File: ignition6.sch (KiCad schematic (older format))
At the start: 9 parts, among them P6 CONN_1, P7 CONN_1, Q1 MOSFET_N, SW1 SWITCH_INV

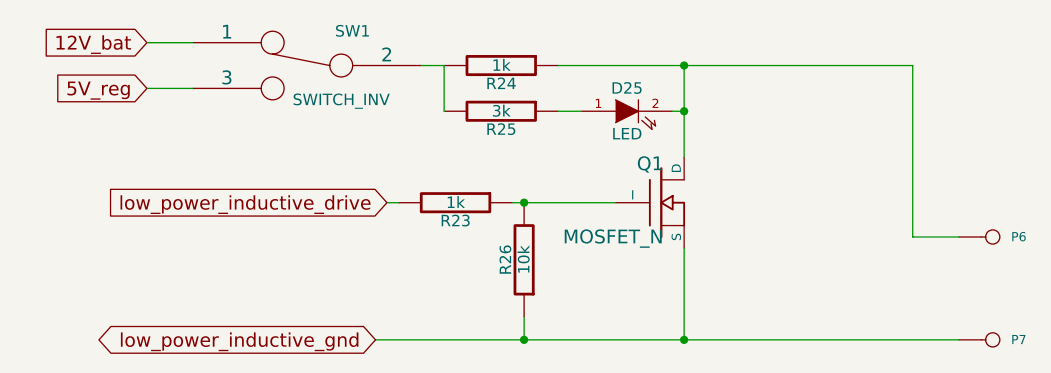
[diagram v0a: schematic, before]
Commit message: Removed LM1815 options. Now adaptive mode and square waves are the default,
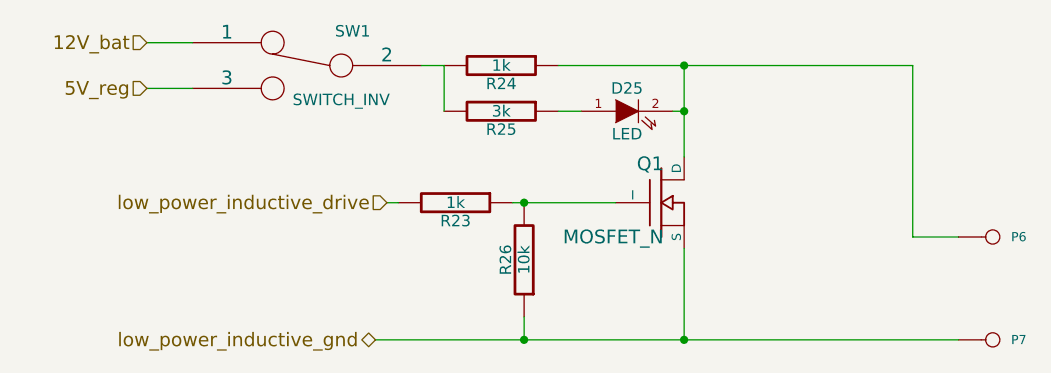
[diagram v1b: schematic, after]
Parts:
- D25: Field1 (none) -> newark,58k2469; Field2 (none) -> vendor1, smd w hem; Field3 (none) -> vendor2, thru w hem; Field4 (none) -> vendor2, smd w hem; Field5 (none) -> x,x; Field6 (none) -> x,x; Field7 (none) -> green; Field8 (none) -> other,more,stuff
- Q1: Field1 (none) -> digi,PIP3104-ND; Field2 (none) -> vendor1, smd w hem; Field3 (none) -> vendor2, thru w hem; Field4 (none) -> vendor2, smd w hem; Field5 (none) -> 8,A; Field6 (none) -> x,x; Field7 (none) -> TOPFET; Field8 (none) -> other,more,stuff
- R23, R24: Field1 (none) -> newark,38k0327; Field2 (none) -> vendor1, smd w hem; Field3 (none) -> vendor2, thru w hem; Field4 (none) -> vendor2, smd w hem; Field5 (none) -> 250,mW; Field6 (none) -> 5,%; Field7 (none) -> carbon film; Field8 (none) -> other,more,stuff
- R25: Field1 (none) -> newark,38k0340; Field2 (none) -> vendor1, smd w hem; Field3 (none) -> vendor2, thru w hem; Field4 (none) -> vendor2, smd w hem; Field5 (none) -> 1/4,W; Field6 (none) -> 5,%; Field7 (none) -> carbon film; Field8 (none) -> other,more,stuff
- R26: Field1 (none) -> newark,38k0328; Field2 (none) -> vendor1, smd w hem; Field3 (none) -> vendor2, thru w hem; Field4 (none) -> vendor2, smd w hem; Field5 (none) -> 250,mW; Field6 (none) -> 5,%; Field7 (none) -> carbon film; Field8 (none) -> other,more,stuff
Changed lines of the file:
@@
-EESchema Schematic File Version 1
-LIBS:power,./freeEMS_lib,device,conn,linear,regul,74xx,cmos4000,adc-dac,memory,xilinx,special,microcontrollers,dsp,microchip,analog_switches,motorola,texas,intel,audio,interface,digital-audio,philips,display,cypress,siliconi,contrib,valves,./freeEMS_1.cache
+EESchema Schematic File Version 2  date Fri 02 Jul 2010 02:24:35 PM ART
+LIBS:power
+LIBS:freeEMS_lib
+LIBS:device
+LIBS:conn
+LIBS:linear
+LIBS:regul
+LIBS:74xx
+LIBS:cmos4000
+LIBS:adc-dac
+LIBS:memory
+LIBS:xilinx
+LIBS:special
+LIBS:microcontrollers
+LIBS:dsp
+LIBS:microchip
+LIBS:analog_switches
+LIBS:motorola
+LIBS:texas
+LIBS:intel
+LIBS:audio
+LIBS:interface
+LIBS:digital-audio
+LIBS:philips
+LIBS:display
+LIBS:cypress
+LIBS:siliconi
+LIBS:contrib
+LIBS:valves
+LIBS:freeEMS_1-cache
 EELAYER 23  0
 EELAYER END
@@
 Sheet 10 41
 Title "freeEMS 1.0"
-Date "15 nov 2008"
+Date "2 jul 2010"
 Rev "A.20"
 Comp "diyefi.org"
@@
 U 1 1 48B16ED5
 P 4000 2050
-F 0 "Q1" H 4010 2220 60  0000 R C
-F 1 "MOSFET_N" H 4010 1900 60  0000 R C
-F 2 "TO220_sm" V 3930 2800 60  0001 C C
-F 4 "digi,PIP3104-ND" V 2130 3800 60  0001 C C
-F 5 "vendor1, smd w hem" V 2130 3800 60  0001 C C
-F 6 "vendor2, thru w hem" V 2130 3800 60  0001 C C
-F 7 "vendor2, smd w hem" V 2130 3800 60  0001 C C
-F 8 "8,A" V 2130 3800 60  0001 C C
-F 9 "x,x" V 2130 3800 60  0001 C C
-F 10 "TOPFET" V 2130 3800 60  0001 C C
-F 11 "other,more,stuff" V 2130 3800 60  0001 C C
+F 0 "Q1" H 4010 2220 60  0000 R CNN
+F 1 "MOSFET_N" H 4010 1900 60  0000 R CNN
+F 2 "TO220_sm" V 3930 2800 60  0001 C CNN
+F 4 "digi,PIP3104-ND" V 2130 3800 60  0001 C CNN "Field1"
+F 5 "vendor1, smd w hem" V 2130 3800 60  0001 C CNN "Field2"
+F 6 "vendor2, thru w hem" V 2130 3800 60  0001 C CNN "Field3"
+F 7 "vendor2, smd w hem" V 2130 3800 60  0001 C CNN "Field4"
+F 8 "8,A" V 2130 3800 60  0001 C CNN "Field5"
+F 9 "x,x" V 2130 3800 60  0001 C CNN "Field6"
+F 10 "TOPFET" V 2130 3800 60  0001 C CNN "Field7"
+F 11 "other,more,stuff" V 2130 3800 60  0001 C CNN "Field8"
 	1    4000 2050
 	1    0    0    -1
@@
 U 1 1 48AE08BB
 P 3400 2300
-F 0 "R26" V 3480 2300 50  0000 C C
-F 1 "10k" V 3400 2300 50  0000 C C
-F 2 "R4-SM0805" V 3580 2400 60  0001 C C
-F 4 "newark,38k0328" V 1230 2850 60  0001 C C
-F 5 "vendor1, smd w hem" V 1230 2850 60  0001 C C
-F 6 "vendor2, thru w hem" V 1230 2850 60  0001 C C
-F 7 "vendor2, smd w hem" V 1230 2850 60  0001 C C
-F 8 "250,mW" V 1230 2850 60  0001 C C
-F 9 "5,%" V 1230 2850 60  0001 C C
-F 10 "carbon film" V 1230 2850 60  0001 C C
-F 11 "other,more,stuff" V 1230 2850 60  0001 C C
+F 0 "R26" V 3480 2300 50  0000 C CNN
+F 1 "10k" V 3400 2300 50  0000 C CNN
+F 2 "R4-SM0805" V 3580 2400 60  0001 C CNN
+F 4 "newark,38k0328" V 1230 2850 60  0001 C CNN "Field1"
+F 5 "vendor1, smd w hem" V 1230 2850 60  0001 C CNN "Field2"
+F 6 "vendor2, thru w hem" V 1230 2850 60  0001 C CNN "Field3"
+F 7 "vendor2, smd w hem" V 1230 2850 60  0001 C CNN "Field4"
+F 8 "250,mW" V 1230 2850 60  0001 C CNN "Field5"
+F 9 "5,%" V 1230 2850 60  0001 C CNN "Field6"
+F 10 "carbon film" V 1230 2850 60  0001 C CNN "Field7"
+F 11 "other,more,stuff" V 1230 2850 60  0001 C CNN "Field8"
 	1    3400 2300
 	-1   0    0    1
@@
 U 1 1 48AE0832
 P 2450 1450
-F 0 "SW1" H 2250 1600 50  0000 C C
-F 1 "SWITCH_INV" H 2300 1300 50  0000 C C
-F 2 "SIL-3" H 2350 1700 60  0001 C C
+F 0 "SW1" H 2250 1600 50  0000 C CNN
+F 1 "SWITCH_INV" H 2300 1300 50  0000 C CNN
+F 2 "SIL-3" H 2350 1700 60  0001 C CNN
 	1    2450 1450
 	-1   0    0    -1
@@
 U 1 1 48AA2529
 P 3850 1650
-F 0 "D25" H 3850 1750 50  0000 C C
-F 1 "LED" H 3850 1550 50  0000 C C
-F 2 "LEDV" V 1680 5050 60  0001 C C
-F 4 "newark,58k2469" V 430 2100 60  0001 C C
-F 5 "vendor1, smd w hem" V 430 2100 60  0001 C C
-F 6 "vendor2, thru w hem" V 430 2100 60  0001 C C
-F 7 "vendor2, smd w hem" V 430 2100 60  0001 C C
-F 8 "x,x" V 430 2100 60  0001 C C
-F 9 "x,x" V 430 2100 60  0001 C C
-F 10 "green" V 430 2100 60  0001 C C
-F 11 "other,more,stuff" V 430 2100 60  0001 C C
+F 0 "D25" H 3850 1750 50  0000 C CNN
+F 1 "LED" H 3850 1550 50  0000 C CNN
+F 2 "LEDV" V 1680 5050 60  0001 C CNN
+F 4 "newark,58k2469" V 430 2100 60  0001 C CNN "Field1"
+F 5 "vendor1, smd w hem" V 430 2100 60  0001 C CNN "Field2"
+F 6 "vendor2, thru w hem" V 430 2100 60  0001 C CNN "Field3"
+F 7 "vendor2, smd w hem" V 430 2100 60  0001 C CNN "Field4"
+F 8 "x,x" V 430 2100 60  0001 C CNN "Field5"
+F 9 "x,x" V 430 2100 60  0001 C CNN "Field6"
+F 10 "green" V 430 2100 60  0001 C CNN "Field7"
+F 11 "other,more,stuff" V 430 2100 60  0001 C CNN "Field8"
 	1    3850 1650
 	1    0    0    -1
@@
 U 1 1 48AA2523
 P 3300 1650
-F 0 "R25" V 3380 1650 50  0000 C C
-F 1 "3k" V 3300 1650 50  0000 C C
-F 2 "R4-SM0805" V 1980 1650 60  0001 C C
-F 4 "newark,38k0340" V -120 2400 60  0001 C C
-F 5 "vendor1, smd w hem" V -120 2400 60  0001 C C
-F 6 "vendor2, thru w hem" V -120 2400 60  0001 C C
-F 7 "vendor2, smd w hem" V -120 2400 60  0001 C C
-F 8 "1/4,W" V -120 2400 60  0001 C C
-F 9 "5,%" V -120 2400 60  0001 C C
-F 10 "carbon film" V -120 2400 60  0001 C C
-F 11 "other,more,stuff" V -120 2400 60  0001 C C
+F 0 "R25" V 3380 1650 50  0000 C CNN
+F 1 "3k" V 3300 1650 50  0000 C CNN
+F 2 "R4-SM0805" V 1980 1650 60  0001 C CNN
+F 4 "newark,38k0340" V -120 2400 60  0001 C CNN "Field1"
+F 5 "vendor1, smd w hem" V -120 2400 60  0001 C CNN "Field2"
+F 6 "vendor2, thru w hem" V -120 2400 60  0001 C CNN "Field3"
+F 7 "vendor2, smd w hem" V -120 2400 60  0001 C CNN "Field4"
+F 8 "1/4,W" V -120 2400 60  0001 C CNN "Field5"
+F 9 "5,%" V -120 2400 60  0001 C CNN "Field6"
+F 10 "carbon film" V -120 2400 60  0001 C CNN "Field7"
+F 11 "other,more,stuff" V -120 2400 60  0001 C CNN "Field8"
 	1    3300 1650
 	0    1    1    0
@@
 U 1 1 48AA1A4E
 P 5450 2650
-F 0 "P7" H 5530 2650 40  0000 L C
-F 1 "CONN_1" H 5450 2705 30  0001 C C
-F 2 "1PIN" V 1880 2850 60  0001 C C
+F 0 "P7" H 5530 2650 40  0000 L CNN
+F 1 "CONN_1" H 5450 2705 30  0001 C CNN
+F 2 "1PIN" V 1880 2850 60  0001 C CNN
 	1    5450 2650
 	1    0    0    -1
@@
 U 1 1 48AA1A4A
 P 5450 2200
-F 0 "P6" H 5530 2200 40  0000 L C
-F 1 "CONN_1" H 5450 2255 30  0001 C C
-F 2 "1PIN" V 1880 2600 60  0001 C C
+F 0 "P6" H 5530 2200 40  0000 L CNN
+F 1 "CONN_1" H 5450 2255 30  0001 C CNN
+F 2 "1PIN" V 1880 2600 60  0001 C CNN
 	1    5450 2200
 	1    0    0    -1
 $EndComp
-Text GLabel 1750 1550 0    60   Input
+Text HLabel 1750 1550 0    60   Input ~ 0
 5V_reg
 $Comp
@@
 U 1 1 489395E6
 P 3100 2050
-F 0 "R23" V 3180 2050 50  0000 C C
-F 1 "1k" V 3100 2050 50  0000 C C
-F 2 "R4-SM0805" V 3280 2150 60  0001 C C
-F 4 "newark,38k0327" V 930 2600 60  0001 C C
-F 5 "vendor1, smd w hem" V 930 2600 60  0001 C C
-F 6 "vendor2, thru w hem" V 930 2600 60  0001 C C
-F 7 "vendor2, smd w hem" V 930 2600 60  0001 C C
-F 8 "250,mW" V 930 2600 60  0001 C C
-F 9 "5,%" V 930 2600 60  0001 C C
-F 10 "carbon film" V 930 2600 60  0001 C C
-F 11 "other,more,stuff" V 930 2600 60  0001 C C
+F 0 "R23" V 3180 2050 50  0000 C CNN
+F 1 "1k" V 3100 2050 50  0000 C CNN
+F 2 "R4-SM0805" V 3280 2150 60  0001 C CNN
+F 4 "newark,38k0327" V 930 2600 60  0001 C CNN "Field1"
+F 5 "vendor1, smd w hem" V 930 2600 60  0001 C CNN "Field2"
+F 6 "vendor2, thru w hem" V 930 2600 60  0001 C CNN "Field3"
+F 7 "vendor2, smd w hem" V 930 2600 60  0001 C CNN "Field4"
+F 8 "250,mW" V 930 2600 60  0001 C CNN "Field5"
+F 9 "5,%" V 930 2600 60  0001 C CNN "Field6"
+F 10 "carbon film" V 930 2600 60  0001 C CNN "Field7"
+F 11 "other,more,stuff" V 930 2600 60  0001 C CNN "Field8"
 	1    3100 2050
 	0    1    1    0
@@
 U 1 1 489395D4
 P 3300 1450
-F 0 "R24" V 3380 1450 50  0000 C C
-F 1 "1k" V 3300 1450 50  0000 C C
-F 2 "R4-SM0805" V 3480 1550 60  0001 C C
-F 4 "newark,38k0327" V 1130 2350 60  0001 C C
-F 5 "vendor1, smd w hem" V 1130 2350 60  0001 C C
-F 6 "vendor2, thru w hem" V 1130 2350 60  0001 C C
-F 7 "vendor2, smd w hem" V 1130 2350 60  0001 C C
-F 8 "250,mW" V 1130 2350 60  0001 C C
-F 9 "5,%" V 1130 2350 60  0001 C C
-F 10 "carbon film" V 1130 2350 60  0001 C C
-F 11 "other,more,stuff" V 1130 2350 60  0001 C C
+F 0 "R24" V 3380 1450 50  0000 C CNN
+F 1 "1k" V 3300 1450 50  0000 C CNN
+F 2 "R4-SM0805" V 3480 1550 60  0001 C CNN
+F 4 "newark,38k0327" V 1130 2350 60  0001 C CNN "Field1"
+F 5 "vendor1, smd w hem" V 1130 2350 60  0001 C CNN "Field2"
+F 6 "vendor2, thru w hem" V 1130 2350 60  0001 C CNN "Field3"
+F 7 "vendor2, smd w hem" V 1130 2350 60  0001 C CNN "Field4"
+F 8 "250,mW" V 1130 2350 60  0001 C CNN "Field5"
+F 9 "5,%" V 1130 2350 60  0001 C CNN "Field6"
+F 10 "carbon film" V 1130 2350 60  0001 C CNN "Field7"
+F 11 "other,more,stuff" V 1130 2350 60  0001 C CNN "Field8"
 	1    3300 1450
 	0    1    1    0
 $EndComp
-Text GLabel 1750 1350 0    60   Input
+Text HLabel 1750 1350 0    60   Input ~ 0
 12V_bat
-Text GLabel 2750 2650 0    60   BiDi
+Text HLabel 2750 2650 0    60   BiDi ~ 0
 low_power_inductive_gnd
-Text GLabel 2800 2050 0    60   Input
+Text HLabel 2800 2050 0    60   Input ~ 0
 low_power_inductive_drive
 $EndSCHEMATC

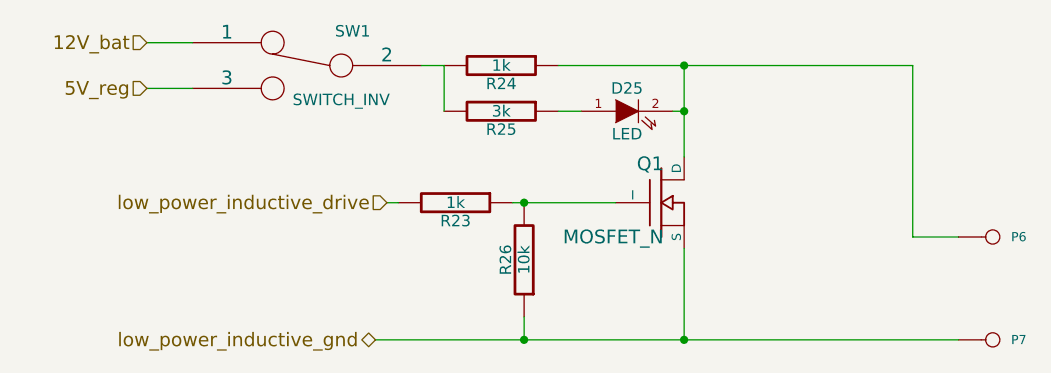
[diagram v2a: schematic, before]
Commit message: Implemented P&H, removed current sense circuitry, removed all unnecessary files from the repo
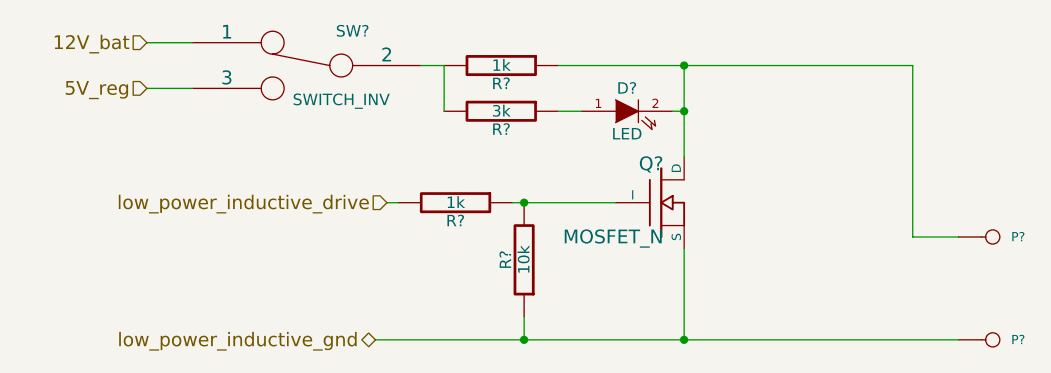
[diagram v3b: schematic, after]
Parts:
- R?: renamed from R26; Field1 newark,38k0328 -> newark,38K0328
- renumbered D25 to D?, P6 to P?, P7 to P?, Q1 to Q?, R24 to R?, R23 to R?, R25 to R?, SW1 to SW?
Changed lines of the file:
@@
-EESchema Schematic File Version 2  date Fri 02 Jul 2010 05:44:26 PM ART
+EESchema Schematic File Version 2  date Sat 03 Jul 2010 10:49:02 AM ART
 LIBS:power
 LIBS:freeEMS_lib
@@
 EELAYER END
 $Descr A4 11700 8267
-Sheet 10 41
+Sheet 1 41
 Title "freeEMS 1.0"
-Date "2 jul 2010"
-Rev "A.20"
+Date "3 jul 2010"
+Rev "A.07"
 Comp "diyefi.org"
 Comment1 "ignition.sch"
@@
 Connection ~ 3400 2050
 $Comp
-L PIP-3104 Q1
+L PIP-3104 Q?
 U 1 1 48B16ED5
 P 4000 2050
-F 0 "Q1" H 4010 2220 60  0000 R CNN
+F 0 "Q?" H 4010 2220 60  0000 R CNN
 F 1 "MOSFET_N" H 4010 1900 60  0000 R CNN
 F 2 "TO220_sm" V 3930 2800 60  0001 C CNN
@@
 $EndComp
 $Comp
-L R R26
+L R R?
 U 1 1 48AE08BB
 P 3400 2300
-F 0 "R26" V 3480 2300 50  0000 C CNN
+F 0 "R?" V 3480 2300 50  0000 C CNN
 F 1 "10k" V 3400 2300 50  0000 C CNN
 F 2 "R4-SM0805" V 3580 2400 60  0001 C CNN
-F 4 "newark,38k0328" V 1230 2850 60  0001 C CNN "Field1"
+F 4 "newark,38K0328" V 1230 2850 60  0001 C CNN "Field1"
 F 5 "vendor1, smd w hem" V 1230 2850 60  0001 C CNN "Field2"
 F 6 "vendor2, thru w hem" V 1230 2850 60  0001 C CNN "Field3"
@@
 $EndComp
 $Comp
-L SWITCH_INV SW1
+L SWITCH_INV SW?
 U 1 1 48AE0832
 P 2450 1450
-F 0 "SW1" H 2250 1600 50  0000 C CNN
+F 0 "SW?" H 2250 1600 50  0000 C CNN
 F 1 "SWITCH_INV" H 2300 1300 50  0000 C CNN
 F 2 "SIL-3" H 2350 1700 60  0001 C CNN
@@
 $EndComp
 $Comp
-L LED D25
+L LED D?
 U 1 1 48AA2529
 P 3850 1650
-F 0 "D25" H 3850 1750 50  0000 C CNN
+F 0 "D?" H 3850 1750 50  0000 C CNN
 F 1 "LED" H 3850 1550 50  0000 C CNN
 F 2 "LEDV" V 1680 5050 60  0001 C CNN
@@
 $EndComp
 $Comp
-L R R25
+L R R?
 U 1 1 48AA2523
 P 3300 1650
-F 0 "R25" V 3380 1650 50  0000 C CNN
+F 0 "R?" V 3380 1650 50  0000 C CNN
 F 1 "3k" V 3300 1650 50  0000 C CNN
 F 2 "R4-SM0805" V 1980 1650 60  0001 C CNN
@@
 $EndComp
 $Comp
-L CONN_1 P7
+L CONN_1 P?
 U 1 1 48AA1A4E
 P 5450 2650
-F 0 "P7" H 5530 2650 40  0000 L CNN
+F 0 "P?" H 5530 2650 40  0000 L CNN
 F 1 "CONN_1" H 5450 2705 30  0001 C CNN
 F 2 "1PIN" V 1880 2850 60  0001 C CNN
@@
 $EndComp
 $Comp
-L CONN_1 P6
+L CONN_1 P?
 U 1 1 48AA1A4A
 P 5450 2200
-F 0 "P6" H 5530 2200 40  0000 L CNN
+F 0 "P?" H 5530 2200 40  0000 L CNN
 F 1 "CONN_1" H 5450 2255 30  0001 C CNN
 F 2 "1PIN" V 1880 2600 60  0001 C CNN
@@
 5V_reg
 $Comp
-L R R23
+L R R?
 U 1 1 489395E6
 P 3100 2050
-F 0 "R23" V 3180 2050 50  0000 C CNN
+F 0 "R?" V 3180 2050 50  0000 C CNN
 F 1 "1k" V 3100 2050 50  0000 C CNN
 F 2 "R4-SM0805" V 3280 2150 60  0001 C CNN
@@
 $EndComp
 $Comp
-L R R24
+L R R?
 U 1 1 489395D4
 P 3300 1450
-F 0 "R24" V 3380 1450 50  0000 C CNN
+F 0 "R?" V 3380 1450 50  0000 C CNN
 F 1 "1k" V 3300 1450 50  0000 C CNN
 F 2 "R4-SM0805" V 3480 1550 60  0001 C CNN

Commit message: Corrected ERC errors by fixing the custom FreeEMS components pinouts
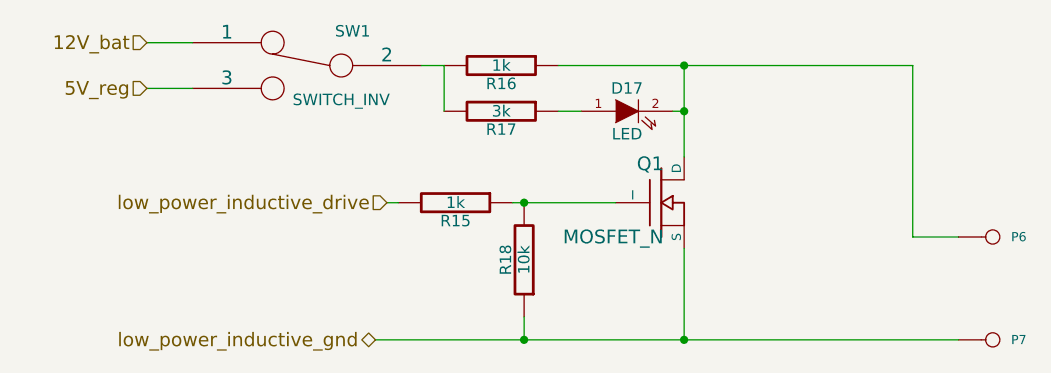
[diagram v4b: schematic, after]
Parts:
- removed D?: LED, LEDV, symbol LED
- removed P? (x2): CONN_1, 1PIN, symbol CONN_1
- removed Q?: MOSFET_N, TO220_sm, symbol PIP-3104
- removed R? (x2): 1k, R4-SM0805, symbol R
- removed R?: 3k, R4-SM0805, symbol R
- removed R?: 10k, R4-SM0805, symbol R
- removed SW?: SWITCH_INV, SIL-3, symbol SWITCH_INV
- added D17: LED, LEDV, symbol LED
- added P6, P7: CONN_1, 1PIN, symbol CONN_1
- added Q1: MOSFET_N, TO220_sm, symbol PIP-3104
- added R15, R16: 1k, R4-SM0805, symbol R
- added R17: 3k, R4-SM0805, symbol R
- added R18: 10k, R4-SM0805, symbol R
- added SW1: SWITCH_INV, SIL-3, symbol SWITCH_INV
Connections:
- net 12V_bat: now also SW1.1
- net 5V_reg: now also SW1.3
- net low_power_inductive_drive: now also R15.2
- net low_power_inductive_gnd: now also P7.1, Q1.3 (S), R18.1
- new net: D17.2 (K), P6.1, Q1.2 (D), R16.1
- new net: R16.2, R17.2, SW1.2
- new net: Q1.1 (I), R15.1, R18.2
- new net: D17.1 (A), R17.1
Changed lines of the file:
@@
-EESchema Schematic File Version 2  date Sat 03 Jul 2010 10:49:02 AM ART
+EESchema Schematic File Version 2  date Sat 03 Jul 2010 12:32:24 PM ART
 LIBS:power
 LIBS:freeEMS_lib
@@
 Connection ~ 3400 2050
 $Comp
-L PIP-3104 Q?
-U 1 1 48B16ED5
+L PIP-3104 Q1
+U 1 1 4C2F5337
 P 4000 2050
-F 0 "Q?" H 4010 2220 60  0000 R CNN
+F 0 "Q1" H 4010 2220 60  0000 R CNN
 F 1 "MOSFET_N" H 4010 1900 60  0000 R CNN
 F 2 "TO220_sm" V 3930 2800 60  0001 C CNN
@@
 $EndComp
 $Comp
-L R R?
-U 1 1 48AE08BB
+L R R18
+U 1 1 4C2F532C
 P 3400 2300
-F 0 "R?" V 3480 2300 50  0000 C CNN
+F 0 "R18" V 3480 2300 50  0000 C CNN
 F 1 "10k" V 3400 2300 50  0000 C CNN
 F 2 "R4-SM0805" V 3580 2400 60  0001 C CNN
@@
 $EndComp
 $Comp
-L SWITCH_INV SW?
-U 1 1 48AE0832
+L SWITCH_INV SW1
+U 1 1 4C2F5327
 P 2450 1450
-F 0 "SW?" H 2250 1600 50  0000 C CNN
+F 0 "SW1" H 2250 1600 50  0000 C CNN
 F 1 "SWITCH_INV" H 2300 1300 50  0000 C CNN
 F 2 "SIL-3" H 2350 1700 60  0001 C CNN
@@
 $EndComp
 $Comp
-L LED D?
-U 1 1 48AA2529
+L LED D17
+U 1 1 4C2F5323
 P 3850 1650
-F 0 "D?" H 3850 1750 50  0000 C CNN
+F 0 "D17" H 3850 1750 50  0000 C CNN
 F 1 "LED" H 3850 1550 50  0000 C CNN
 F 2 "LEDV" V 1680 5050 60  0001 C CNN
@@
 $EndComp
 $Comp
-L R R?
-U 1 1 48AA2523
+L R R17
+U 1 1 4C2F531D
 P 3300 1650
-F 0 "R?" V 3380 1650 50  0000 C CNN
+F 0 "R17" V 3380 1650 50  0000 C CNN
 F 1 "3k" V 3300 1650 50  0000 C CNN
 F 2 "R4-SM0805" V 1980 1650 60  0001 C CNN
@@
 $EndComp
 $Comp
-L CONN_1 P?
-U 1 1 48AA1A4E
+L CONN_1 P7
+U 1 1 4C2F5315
 P 5450 2650
-F 0 "P?" H 5530 2650 40  0000 L CNN
+F 0 "P7" H 5530 2650 40  0000 L CNN
 F 1 "CONN_1" H 5450 2705 30  0001 C CNN
 F 2 "1PIN" V 1880 2850 60  0001 C CNN
@@
 $EndComp
 $Comp
-L CONN_1 P?
-U 1 1 48AA1A4A
+L CONN_1 P6
+U 1 1 4C2F5311
 P 5450 2200
-F 0 "P?" H 5530 2200 40  0000 L CNN
+F 0 "P6" H 5530 2200 40  0000 L CNN
 F 1 "CONN_1" H 5450 2255 30  0001 C CNN
 F 2 "1PIN" V 1880 2600 60  0001 C CNN
@@
 5V_reg
 $Comp
-L R R?
-U 1 1 489395E6
+L R R15
+U 1 1 4C2F52E7
 P 3100 2050
-F 0 "R?" V 3180 2050 50  0000 C CNN
+F 0 "R15" V 3180 2050 50  0000 C CNN
 F 1 "1k" V 3100 2050 50  0000 C CNN
 F 2 "R4-SM0805" V 3280 2150 60  0001 C CNN
@@
 $EndComp
 $Comp
-L R R?
-U 1 1 489395D4
+L R R16
+U 1 1 4C2F52E0
 P 3300 1450
-F 0 "R?" V 3380 1450 50  0000 C CNN
+F 0 "R16" V 3380 1450 50  0000 C CNN
 F 1 "1k" V 3300 1450 50  0000 C CNN
 F 2 "R4-SM0805" V 3480 1550 60  0001 C CNN
